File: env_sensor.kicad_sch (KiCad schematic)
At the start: 41 parts, among them J1 E Paper, J10 PWMOUT, J15 MH-Z19, J16 ADCs, J18 Conn_01x02_Pin, J3 Barrel_Jack, J4 LED_OUTPUT, J6 ADCs, J7 USB_C_Receptacle_USB2.0_16P, J8 v5_v3, J9 DEBUG, Q1 NMOS, Q2 NMOS, Q3 NMOS, SW1 EN, SW2 BOOT, U3 ESP32-S3-WROOM-1, U4 TXB0104PW, U6 TPS2065CDBV, U7 AP7361C-33E, Y1 Crystal

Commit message: update
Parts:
- removed D4: POWER, LED_SMD:LED_0603_1608Metric, symbol Device:LED
- removed J6: ADCs, Connector_PinSocket_2.54mm:PinSocket_1x04_P2.54mm_Vertical, symbol Connector:Conn_01x04_Socket
- removed J8: v5_v3, Connector_PinSocket_2.54mm:PinSocket_1x03_P2.54mm_Vertical, symbol Connector:Conn_01x03_Socket
- removed R7: 1k, Resistor_SMD:R_0603_1608Metric, symbol Device:R
- added D5: POWER, LED_SMD:LED_0603_1608Metric, symbol Device:LED
- added J13: Conn_01x03_Socket, Connector_PinHeader_2.54mm:PinHeader_1x03_P2.54mm_Vertical, symbol Connector:Conn_01x03_Socket
- added J6: Conn_01x08_Socket, Connector_PinSocket_2.54mm:PinSocket_2x04_P2.54mm_Vertical, symbol Connector:Conn_01x08_Socket
- added R3: 1k, Resistor_SMD:R_0603_1608Metric, symbol Device:R
- J10: footprint Connector_PinSocket_2.54mm:PinSocket_1x06_P2.54mm_Vertical -> Connector_PinHeader_2.54mm:PinHeader_1x06_P2.54mm_Vertical
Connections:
- net VServo is gone; now on net VCC: C6.1, J10.2 (Pin_2), U4.14 (VCCB)
- net GND: now also J13.3 (Pin_3), J6.7 (Pin_7), J6.8 (Pin_8), R3.1
- net IO6: now also J6.5 (Pin_5)
- net v3v: now also D5.2 (A), J6.1 (Pin_1)
- net IO38: now reaches U3.31 (IO38)
- net IO38: now also J6.2 (Pin_2)
- net at U3.36 (RXD0): now also J13.2 (Pin_2)
- net at U3.37 (TXD0): now also J13.1 (Pin_1)
- net IO7: now reaches U3.7 (IO7)
- net IO7: now also J6.6 (Pin_6)
- net SCL renamed IO14
- net IO14: now also J6.4 (Pin_4)
- net SDA renamed IO13
- net IO13: now also J6.3 (Pin_3)
- new net: D5.1 (K), R3.2

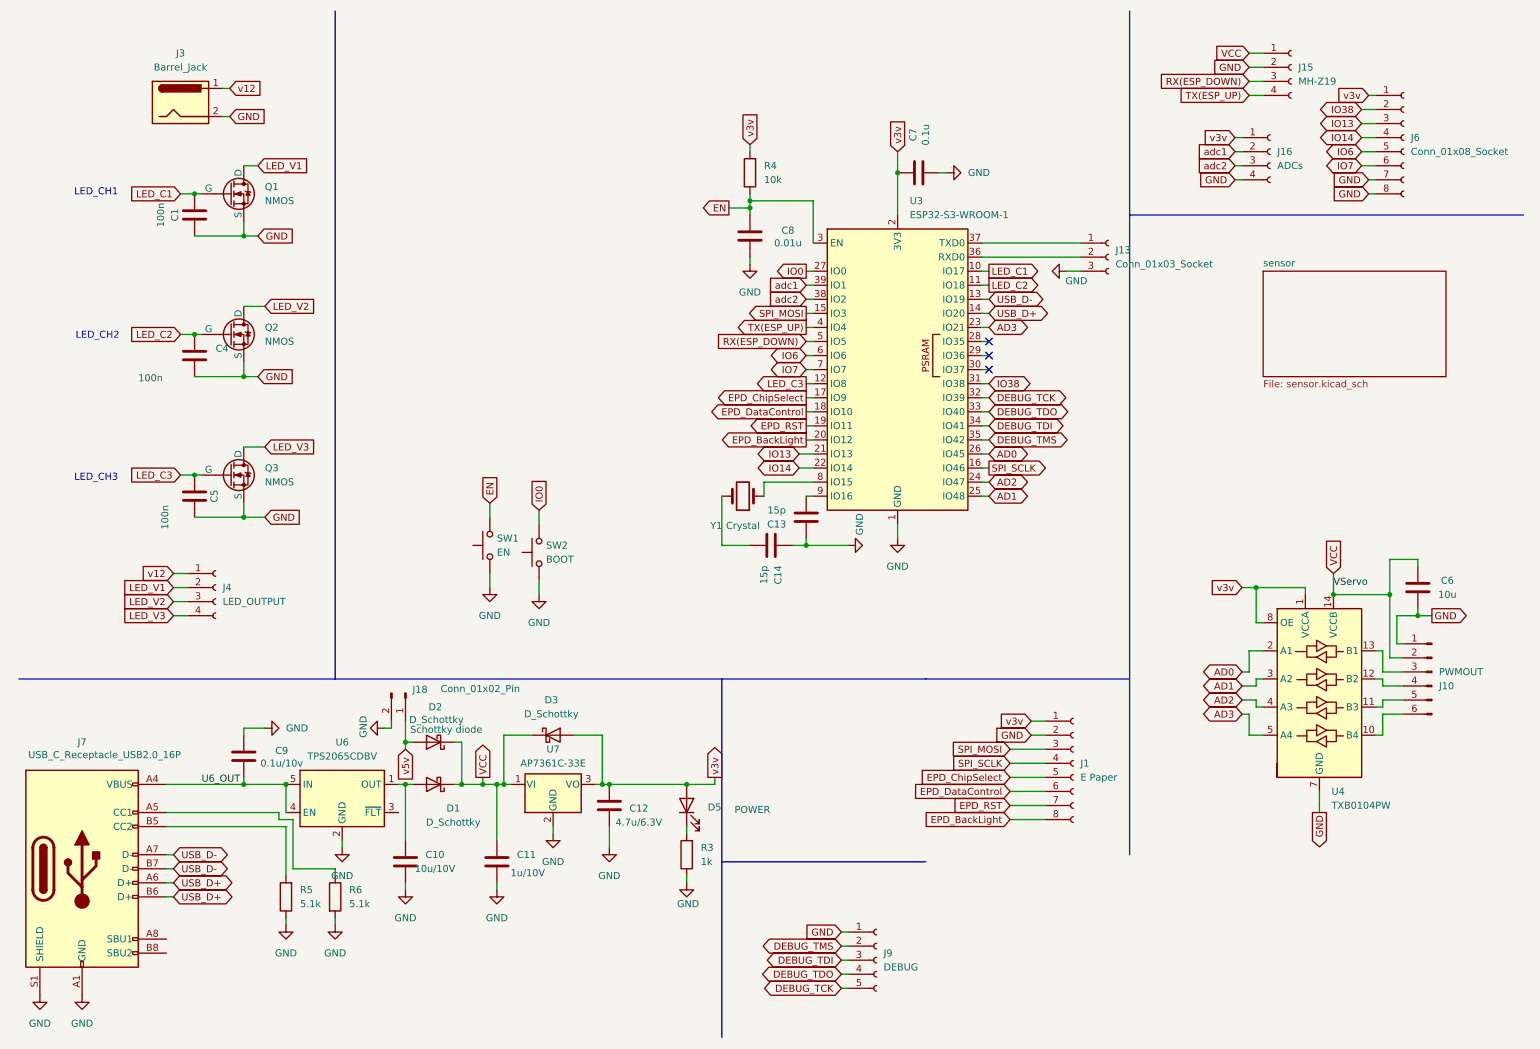
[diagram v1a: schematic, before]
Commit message: delete extension board
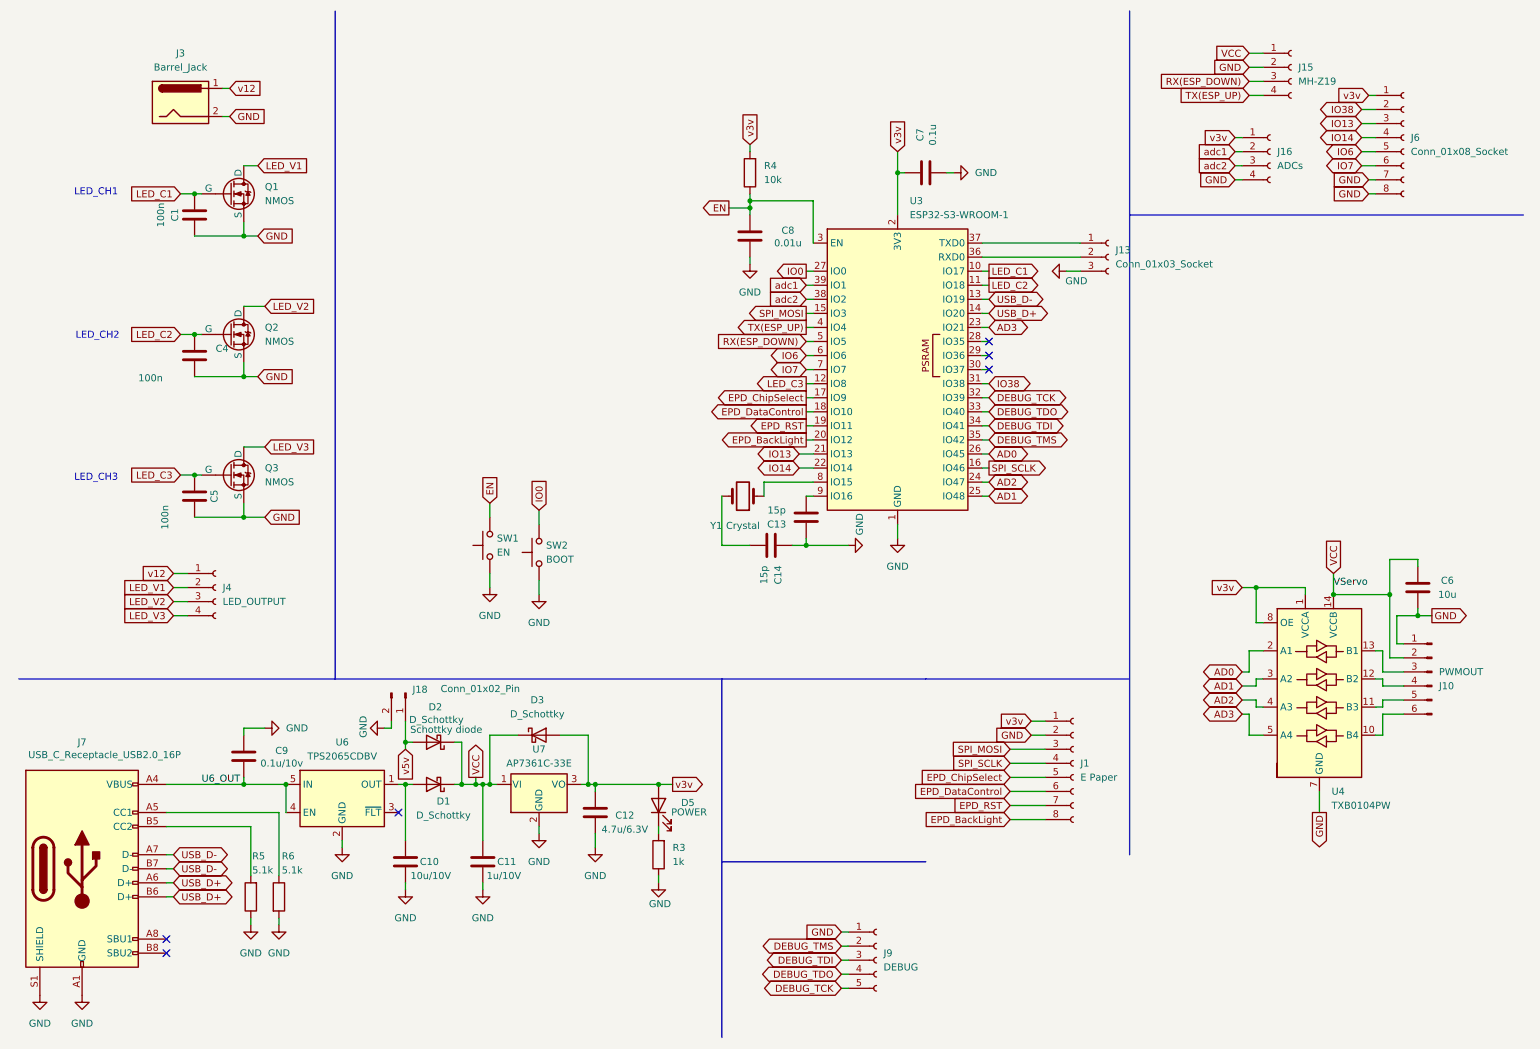
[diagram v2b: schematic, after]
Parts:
- C1, C4, C5, C7, C9: LCSC C1525 -> C14663
- C11: LCSC C363553 -> C15849
- C12: LCSC C380326 -> C19666
- C13, C14: LCSC C5360831 -> C1644
- C8: LCSC C136131 -> C57112
- D5: LCSC C3030991 -> C2286
- J13, J6: now left out of the parts list
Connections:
- no-connect marks 3 -> 6
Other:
- removed sheet sensor
- moved on the sheet: C11, C12, C7, D3, D5, R3, R5, R6, U7
